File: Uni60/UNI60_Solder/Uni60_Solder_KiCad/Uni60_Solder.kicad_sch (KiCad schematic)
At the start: 183 parts, among them J1 Conn_01x04, SW1 SW_Push, SW2 SW_Push, U1 STM32F072CBTx, U2 XC6206PxxxMR, U3 USBLC6-2SC6

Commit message: aadded full 2.75u rshift support
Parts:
- added KC_RSFT_2.75u, KC_SPC_6.25U1: MX_SW_solder, shentobento:SW_MX_1u, symbol shentobento:MX_SW_solder
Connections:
- net COL12: now also KC_RSFT_2.75u.1
- net COL6: now also KC_SPC_6.25U1.1
- net at D59.2 (A), KC_SPC1.2, KC_SPC_2.75U1.2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: now also KC_SPC_6.25U1.2
- net at D54.2 (A), KC_RSFT1.2: now also KC_RSFT_2.75u.2
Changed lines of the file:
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@@
 	)
 	(junction
+		(at 238.76 97.79)
+		(diameter 0)
+		(color 0 0 0 0)
+	)
+	(junction
 		(at 147.32 105.41)
 		(diameter 0)
@@
 	)
 	(junction
+		(at 182.88 110.49)
+		(diameter 0)
+		(color 0 0 0 0)
+	)
+	(junction
 		(at 111.76 92.71)
 		(diameter 0)
@@
 	)
 	(junction
+		(at 187.96 115.57)
+		(diameter 0)
+		(color 0 0 0 0)
+	)
+	(junction
 		(at 162.56 39.37)
 		(diameter 0)
@@
 	(wire
 		(pts
+			(xy 238.76 97.79) (xy 242.57 97.79)
+		)
+		(stroke
+			(width 0)
+			(type default)
+		)
+	)
+	(wire
+		(pts
 			(xy 187.96 105.41) (xy 198.12 105.41)
 		)
@@
 	(wire
 		(pts
+			(xy 233.68 92.71) (xy 237.49 92.71)
+		)
+		(stroke
+			(width 0)
+			(type default)
+		)
+	)
+	(wire
+		(pts
+			(xy 187.96 115.57) (xy 191.77 115.57)
+		)
+		(stroke
+			(width 0)
+			(type default)
+		)
+	)
+	(wire
+		(pts
 			(xy 121.92 74.93) (xy 121.92 92.71)
 		)
@@
 	(wire
 		(pts
+			(xy 182.88 110.49) (xy 186.69 110.49)
+		)
+		(stroke
+			(width 0)
+			(type default)
+		)
+	)
+	(wire
+		(pts
 			(xy 137.16 105.41) (xy 147.32 105.41)
 		)
@@
 	(symbol
 		(lib_id "shentobento:MX_SW_solder")
+		(at 240.03 95.25 0)
+		(unit 1)
+		(body_style 1)
+		(exclude_from_sim no)
+		(in_bom yes)
+		(on_board yes)
+		(in_pos_files yes)
+		(dnp no)
+		(fields_autoplaced yes)
+		(property "Reference" "KC_RSFT_2.75u"
+			(at 240.03 90.17 0)
+			(hide yes)
+			(show_name no)
+			(do_not_autoplace no)
+			(effects
+				(font
+					(size 1.27 1.27)
+				)
+			)
+		)
+		(property "Value" "MX_SW_solder"
+			(at 240.03 90.17 0)
+			(hide yes)
+			(show_name no)
+			(do_not_autoplace no)
+			(effects
+				(font
+					(size 1.27 1.27)
+				)
+			)
+		)
+		(property "Footprint" "shentobento:SW_MX_1u"
+			(at 240.03 95.25 0)
+			(hide yes)
+			(show_name no)
+			(do_not_autoplace no)
+			(effects
+				(font
+					(size 1.27 1.27)
+				)
+			)
+		)
+		(property "Datasheet" ""
+			(at 240.03 95.25 0)
+			(hide yes)
+			(show_name no)
+			(do_not_autoplace no)
+			(effects
+				(font
+					(size 1.27 1.27)
+				)
+			)
+		)
+		(property "Description" "Push button switch, normally open, two pins, 45° tilted"
+			(at 240.03 95.25 0)
+			(hide yes)
+			(show_name no)
+			(do_not_autoplace no)
+			(effects
+				(font
+					(size 1.27 1.27)
+				)
+			)
+		)
+		(pin "1"
+		)
+		(pin "2"
+		)
+		(instances
+			(project "Uni60_Solder"
+				(path "/e464f1d1-4c01-4fad-a203-20008a0f30b7"
+					(reference "KC_RSFT_2.75u")
+					(unit 1)
+				)
+			)
+		)
+	)
+	(symbol
+		(lib_id "shentobento:MX_SW_solder")
 		(at 252.73 59.69 0)
 		(unit 1)
@@
 					(unit 1)
 				)
+			)
+		)
+	)
+	(symbol
+		(lib_id "shentobento:MX_SW_solder")
+		(at 189.23 113.03 0)
+		(unit 1)
+		(body_style 1)
+		(exclude_from_sim no)
+		(in_bom yes)
+		(on_board yes)
+		(in_pos_files yes)
+		(dnp no)
+		(fields_autoplaced yes)
+		(property "Reference" "KC_SPC_6.25U1"
+			(at 189.23 107.95 0)
+			(hide yes)
+			(show_name no)
+			(do_not_autoplace no)
+			(effects
+				(font
+					(size 1.27 1.27)
+				)
+			)
+		)
+		(property "Value" "MX_SW_solder"
+			(at 189.23 107.95 0)
+			(hide yes)
+			(show_name no)
+			(do_not_autoplace no)
+			(effects
+				(font
+					(size 1.27 1.27)
+				)
+			)
+		)
+		(property "Footprint" "shentobento:SW_MX_1u"
+			(at 189.23 113.03 0)
+			(hide yes)
+			(show_name no)
+			(do_not_autoplace no)
+			(effects
+				(font
+					(size 1.27 1.27)
+				)
+			)
+		)
+		(property "Datasheet" ""
+			(at 189.23 113.03 0)
+			(hide yes)
+			(show_name no)
+			(do_not_autoplace no)
+			(effects
+				(font
+					(size 1.27 1.27)
+				)
+			)
+		)
+		(property "Description" "Push button switch, normally open, two pins, 45° tilted"
+			(at 189.23 113.03 0)
+			(hide yes)
+			(show_name no)
+			(do_not_autoplace no)
+			(effects
+				(font
+					(size 1.27 1.27)
+				)
+			)
+		)
+		(pin "1"
+		)
+		(pin "2"
+		)
+		(instances
+			(project "Uni60_Solder"
+				(path "/e464f1d1-4c01-4fad-a203-20008a0f30b7"
+					(reference "KC_SPC_6.25U1")
+					(unit 1)
+				)

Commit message: Update Uni60_Solder.kicad_sch
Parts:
- renumbered KC_RSFT_2.75u to KC_RSFT_2.75u1
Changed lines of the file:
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@@
 		(dnp no)
 		(fields_autoplaced yes)
-		(property "Reference" "KC_RSFT_2.75u"
+		(property "Reference" "KC_RSFT_2.75u1"
 			(at 240.03 90.17 0)
 			(hide yes)
@@
 			(project "Uni60_Solder"
 				(path "/e464f1d1-4c01-4fad-a203-20008a0f30b7"
-					(reference "KC_RSFT_2.75u")
+					(reference "KC_RSFT_2.75u1")
 					(unit 1)
 				)

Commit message: Update Uni60_Solder.kicad_sch
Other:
- title: Velvet Pro Solder PCB v1.0.0 by ShentoBento -> Uni60 PCB v1.0.0 by ShentoBento
- moved on the sheet: C7, C8, GND1, J1, U2, U3

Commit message: idk what changed tbh
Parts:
- added J2, J3, J4: Conn_01x04, shentobento:JST_SH_1x04, symbol shentobento:Conn_01x04
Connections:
- net +5V: now also J2.1 (Pin_1), J3.1 (Pin_1), J4.1 (Pin_1)
- net GND: now also J2.4 (Pin_4), J3.4 (Pin_4), J4.4 (Pin_4)
- net USB_D+: now also J2.3 (Pin_3), J3.3 (Pin_3), J4.3 (Pin_3)
- net USB_D-: now also J2.2 (Pin_2), J3.2 (Pin_2), J4.2 (Pin_2)
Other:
- moved on the sheet: C7, C8, U2, U3

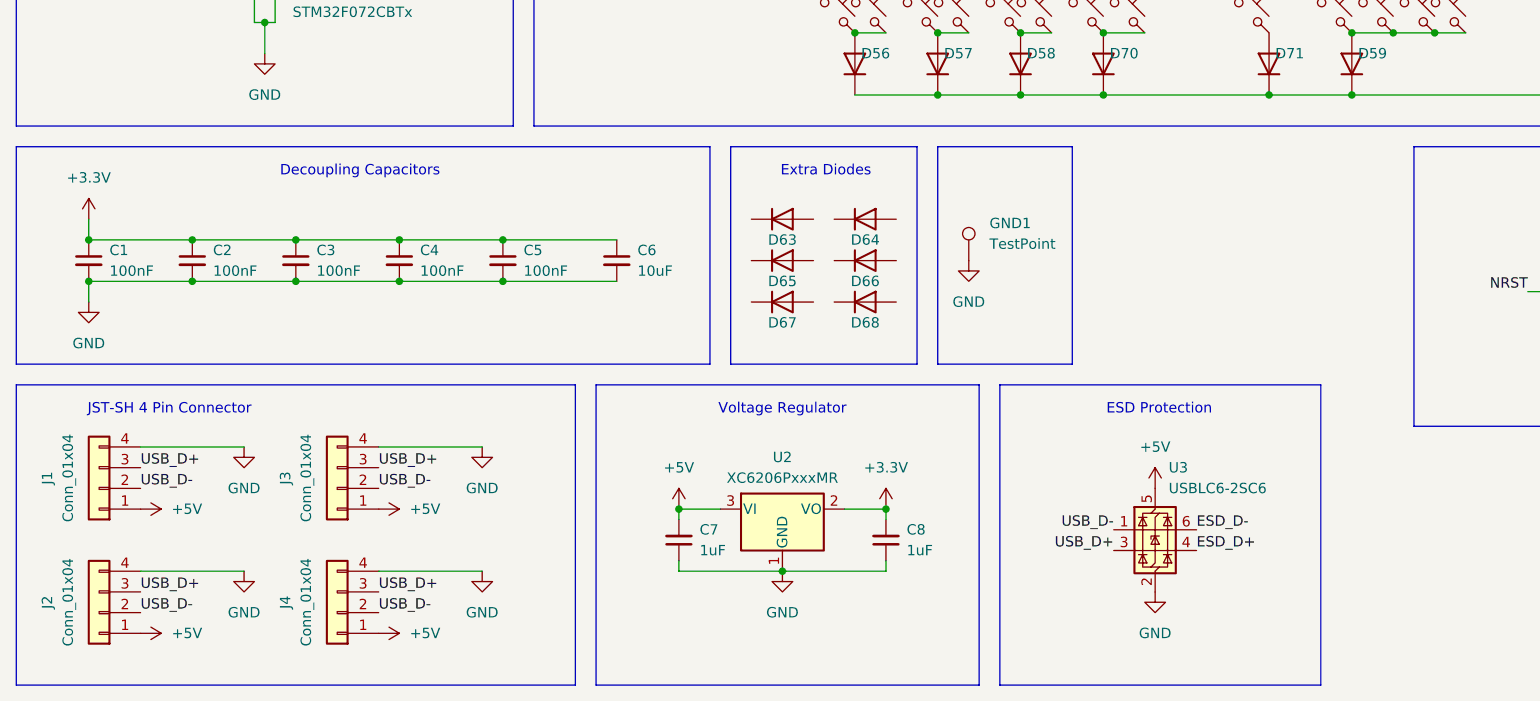
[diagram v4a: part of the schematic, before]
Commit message: added stinga support
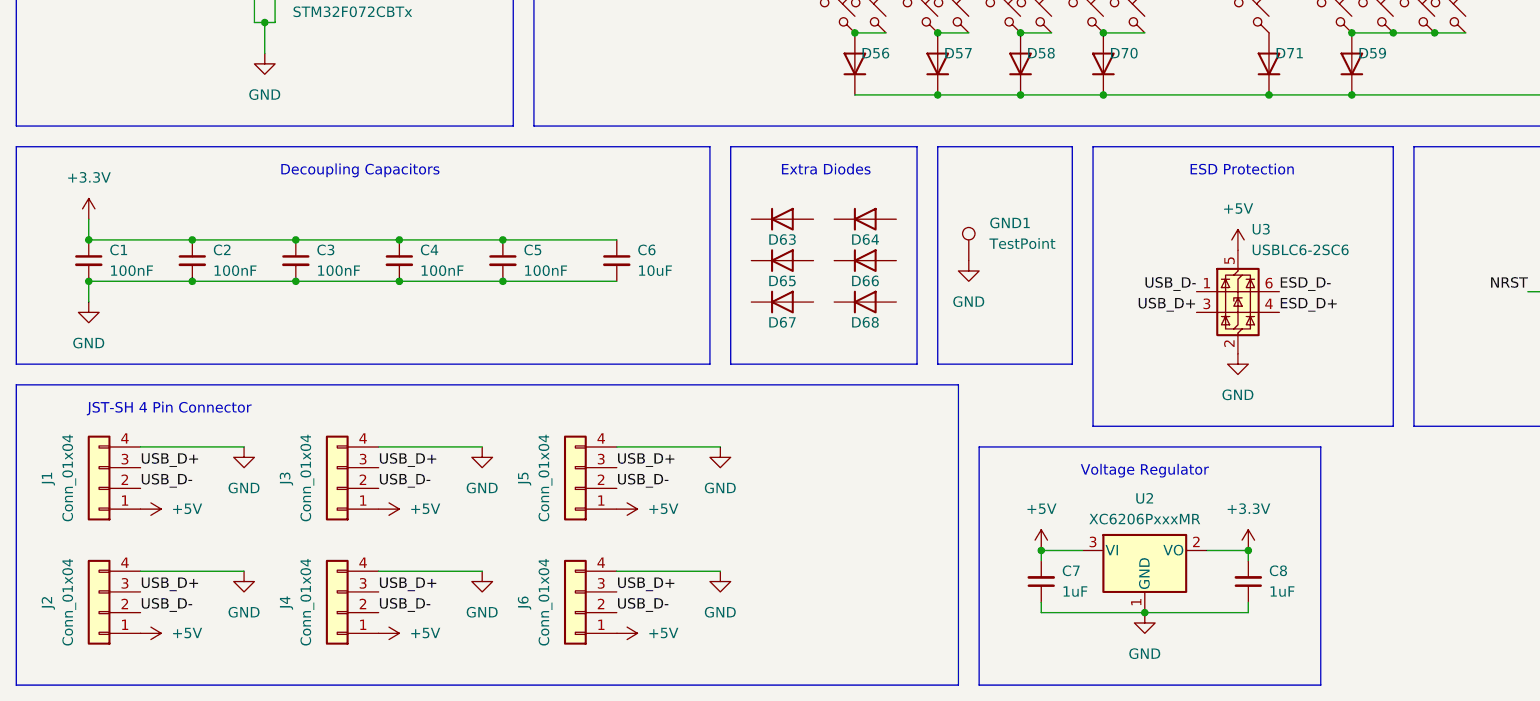
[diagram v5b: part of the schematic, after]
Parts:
- added J5: Conn_01x04, shentobento:JST_SH_1x04, symbol shentobento:Conn_01x04
- added J6: Conn_01x04, Connector_Molex:Molex_Pico-EZmate_78171-0004_1x04-1MP_P1.20mm_Vertical, symbol shentobento:Conn_01x04
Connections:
- net +5V: now also J5.1 (Pin_1), J6.1 (Pin_1)
- net GND: now also J5.4 (Pin_4), J6.4 (Pin_4)
- net USB_D+: now also J5.3 (Pin_3), J6.3 (Pin_3)
- net USB_D-: now also J5.2 (Pin_2), J6.2 (Pin_2)
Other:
- moved on the sheet: C7, C8, U2, U3

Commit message: added molex connector to my library
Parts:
- J6: footprint Connector_Molex:Molex_Pico-EZmate_78171-0004_1x04-1MP_P1.20mm_Vertical -> shentobento:Molex_Pico-EZmate_78171-0004_1x04-1MP_P1.20mm_Vertical
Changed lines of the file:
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@@
 			)
 		)
-		(property "Footprint" "Connector_Molex:Molex_Pico-EZmate_78171-0004_1x04-1MP_P1.20mm_Vertical"
+		(property "Footprint" "shentobento:Molex_Pico-EZmate_78171-0004_1x04-1MP_P1.20mm_Vertical"
 			(at 82.55 186.69 0)
 			(hide yes)

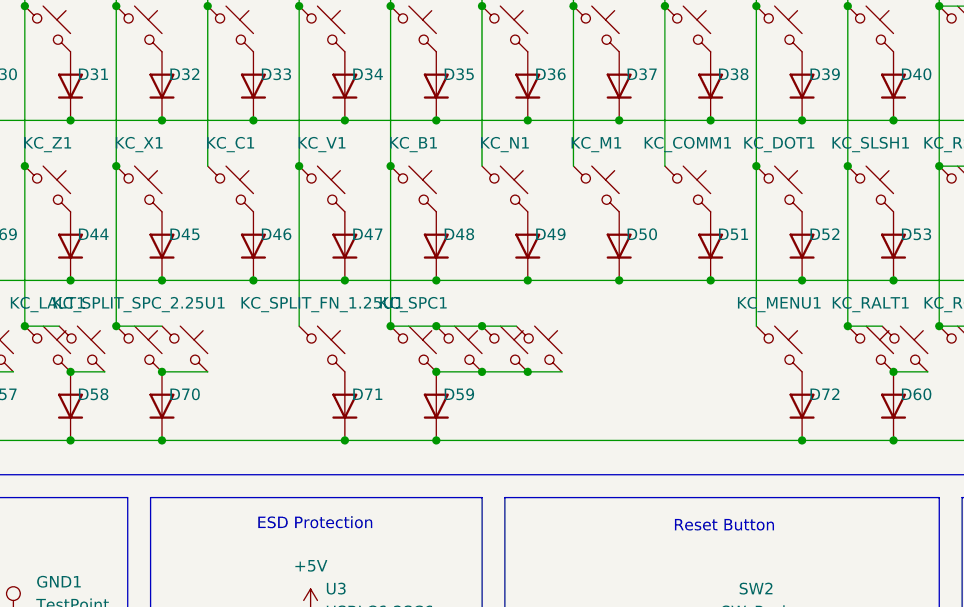
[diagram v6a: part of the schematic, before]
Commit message: changed hole ID sizes to 1.55mm
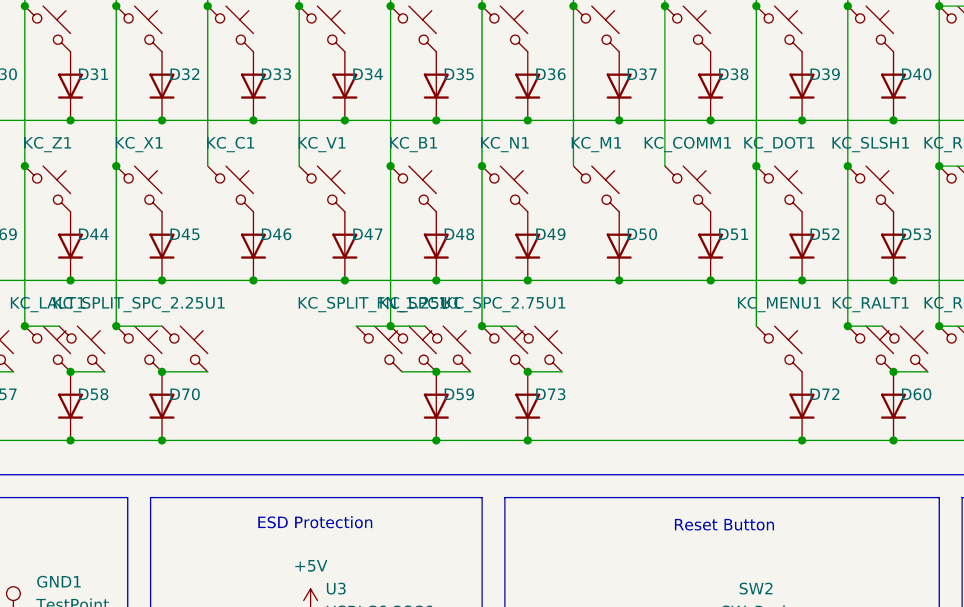
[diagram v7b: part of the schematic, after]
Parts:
- removed D71: 1N4148, shentobento:D_SOD-123, symbol shentobento:1N4148
- added D73: 1N4148, shentobento:D_SOD-123, symbol shentobento:1N4148
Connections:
- net COL5: no longer KC_SPLIT_FN_1.25U1.1
- net COL6: now also KC_SPLIT_FN_1.25U1.1; no longer KC_SPC_2.75U1.1, KC_SPC_3U1.1
- net COL7: now also KC_SPC_2.75U1.1, KC_SPC_3U1.1
- net ROW4: now also D73.1 (K)
- net at D59.2 (A), KC_SPC1.2, KC_SPC_6.25U1.2: now also KC_SPLIT_FN_1.25U1.2; no longer KC_SPC_2.75U1.2, KC_SPC_3U1.2
- new net: D73.2 (A), KC_SPC_2.75U1.2, KC_SPC_3U1.2
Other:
- moved on the sheet: KC_SPLIT_FN_1.25U1

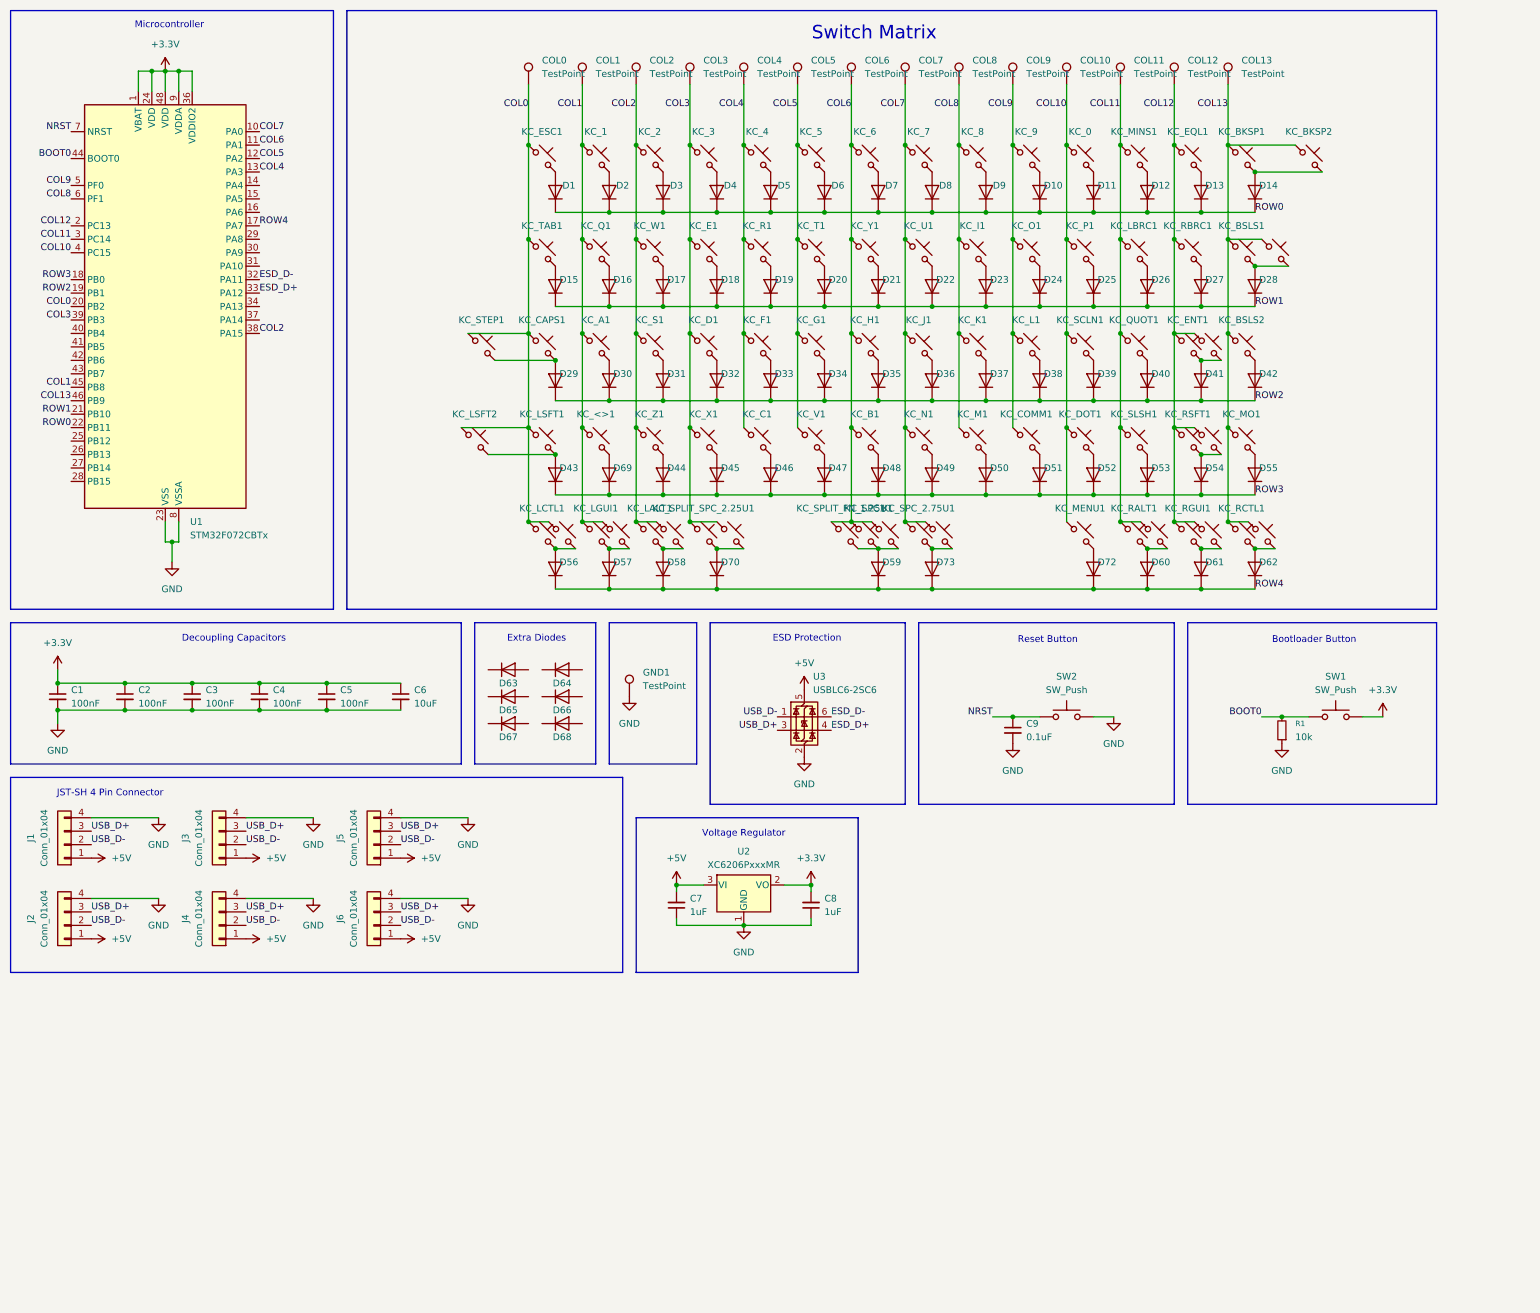
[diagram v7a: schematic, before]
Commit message: fixed traces
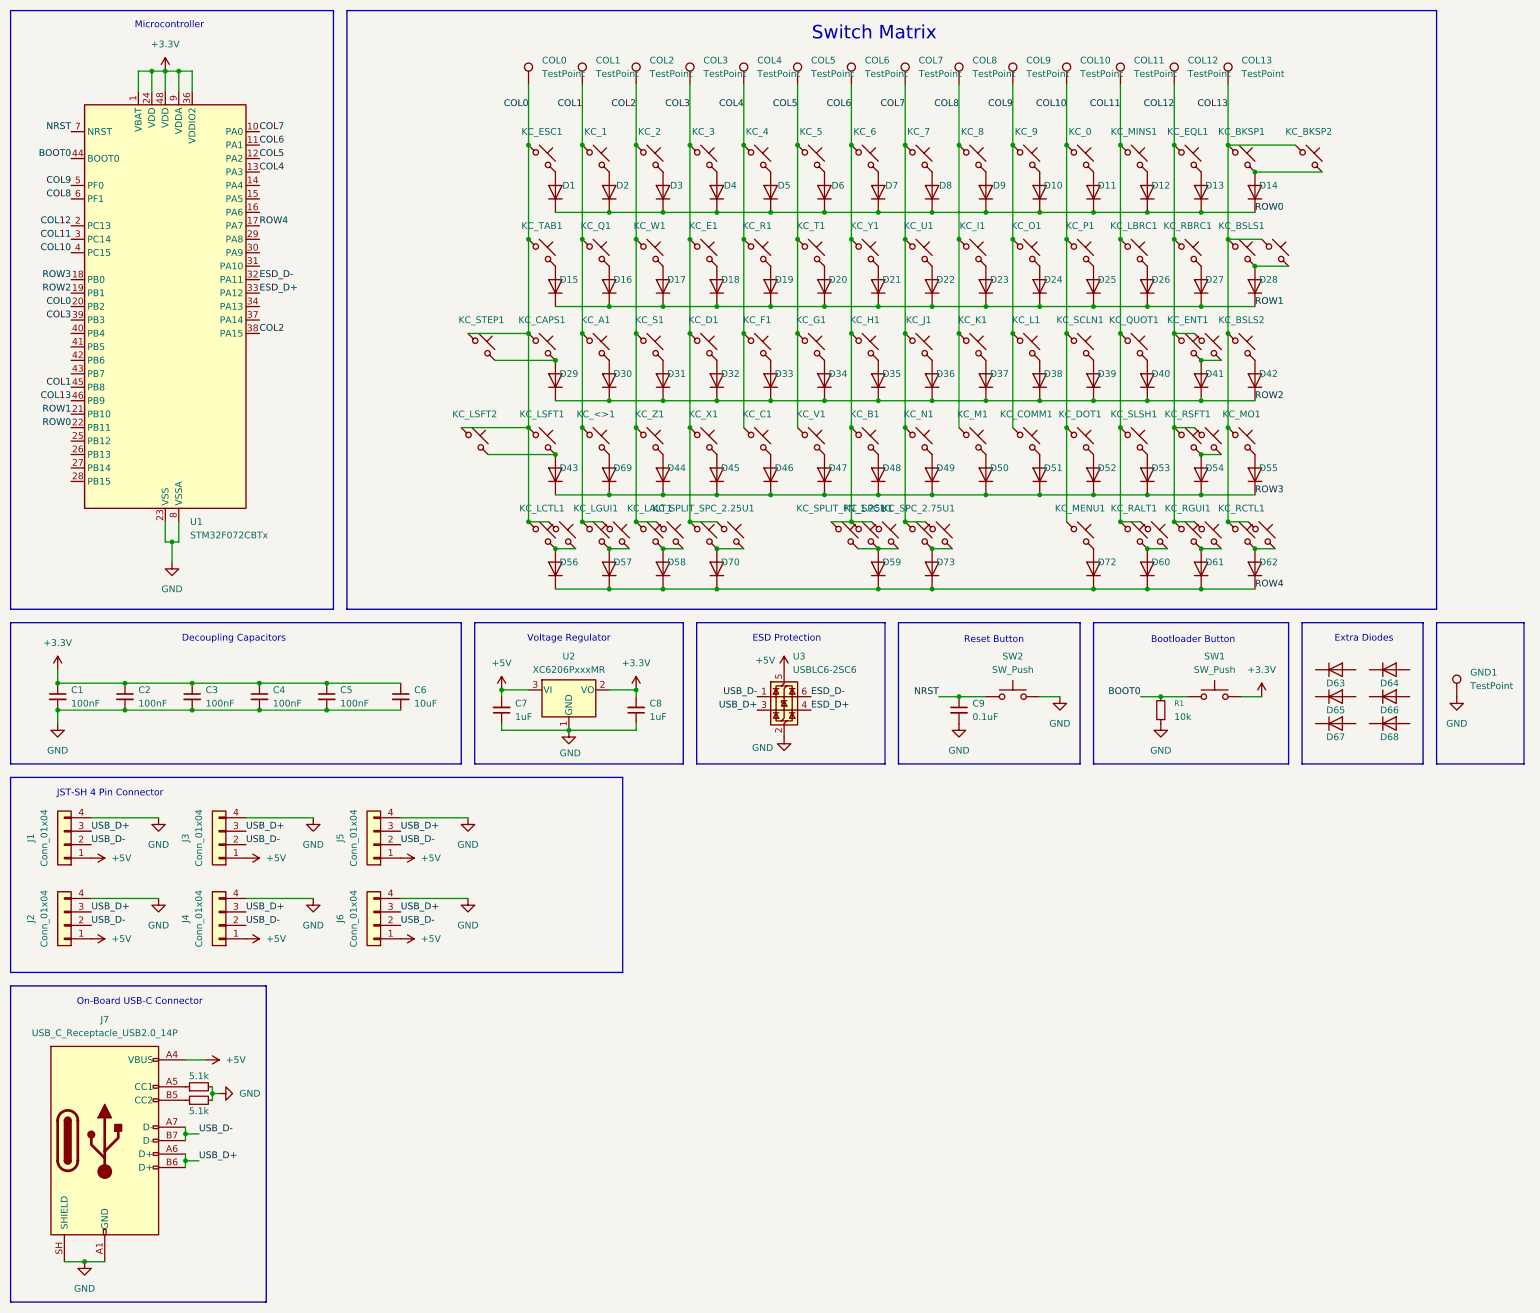
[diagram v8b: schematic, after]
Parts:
- added J7: USB_C_Receptacle_USB2.0_14P, Connector_USB:USB_C_Receptacle_GCT_USB4105-xx-A_16P_TopMnt_Horizontal, symbol Connector:USB_C_Receptacle_USB2.0_14P
- added R2, R3: 5.1k, shentobento:R_0201_0603Metric, symbol shentobento:R_Small
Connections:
- net +5V: now also J7.A4 (VBUS), J7.A9 (VBUS), J7.B4 (VBUS), J7.B9 (VBUS)
- net GND: now also J7.A1 (GND), J7.A12 (GND), J7.B1 (GND), J7.B12 (GND), J7.SH (SHIELD), R2.2, R3.2
- net USB_D+: now also J7.A6 (D+), J7.B6 (D+)
- net USB_D-: now also J7.A7 (D-), J7.B7 (D-)
- new net: J7.A5 (CC1), R2.1
- new net: J7.B5 (CC2), R3.1
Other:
- note added: "On-Board USB-C Connector"
- moved on the sheet: C7, C8, C9, D63, D64, D65, D66, D67, D68, GND1, R1, SW1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
